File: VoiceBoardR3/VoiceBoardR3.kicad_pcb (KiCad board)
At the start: 4 copper layers, 130 x 50 mm, 170 parts, among them Q201 BC857, Q202 BC857, Q301 BC858, Q302 BC858, Q401 BC857, Q402 BC857, Q403 BC847, Q404 BC857, Q405 BC847, Q406 BC857, U101 TMUX4053, U102 TMUX4053, U103 VoiceBoardConn_18P_254P, U201 TL074, U202 TL074, U203 MCP4451-104E-ST, U204 TL074, U205 MCP4451-104E-ST, U206 TL072, U301 TL074, U302 MCP45HV51-ST, U303 LM13700, U402 LM13700, U403 TL074, U404 TL074

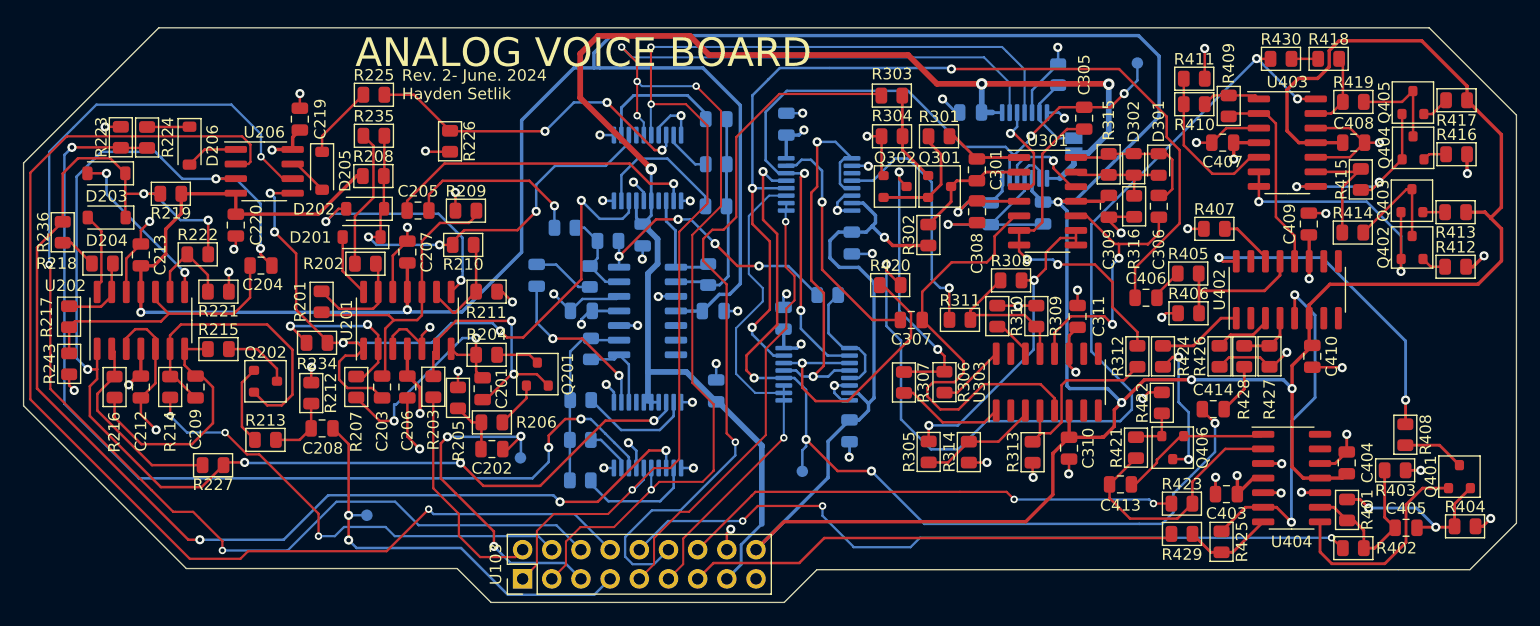
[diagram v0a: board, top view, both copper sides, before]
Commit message: separate power supply board
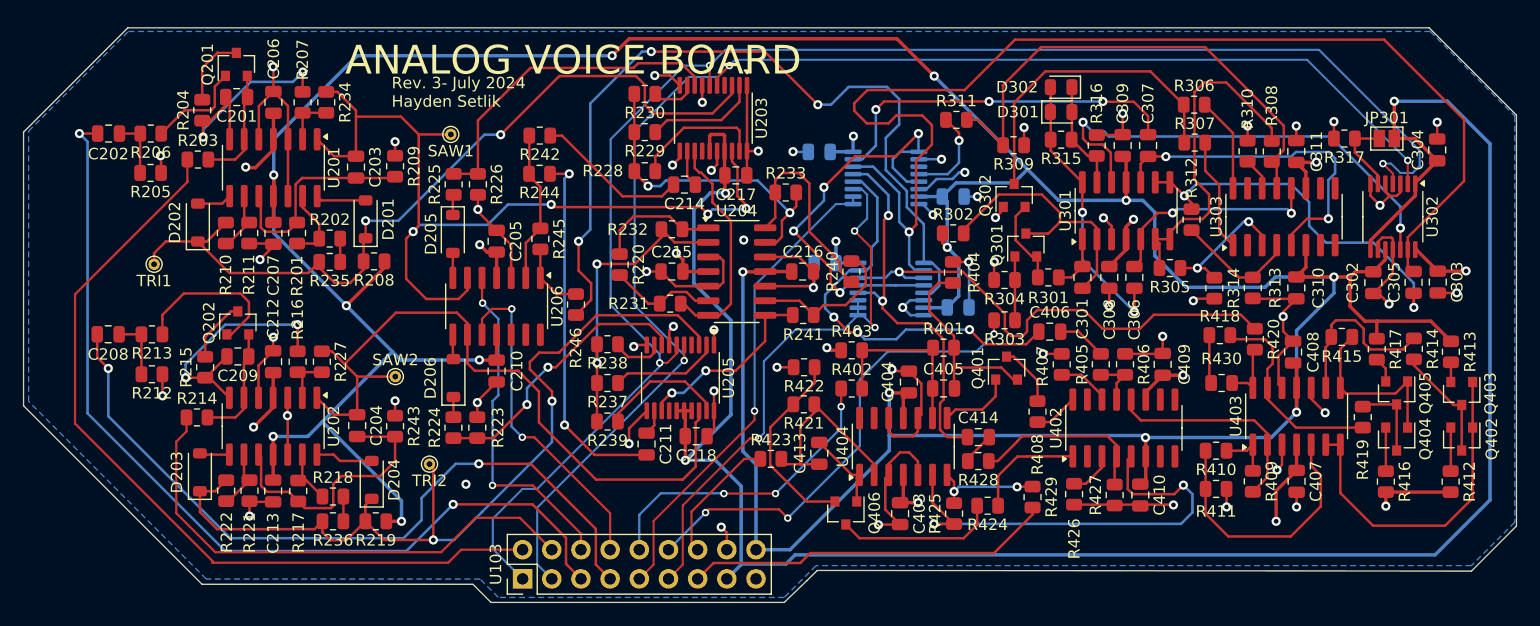
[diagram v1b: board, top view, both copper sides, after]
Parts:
- removed C219, C220: 100n, Capacitor_SMD:C_0805_2012Metric
- removed TP101: FLTR_OUT, TestPoint:TestPoint_Pad_D1.0mm_Value
- removed TP102: VCA_IN, TestPoint:TestPoint_Pad_D1.0mm_Value
- removed TP103: CLK_2, TestPoint:TestPoint_Pad_D1.0mm_Value
- removed TP104: CLK_1, TestPoint:TestPoint_Pad_D1.0mm_Value
- added C211: 1u, Capacitor_SMD:C_0805_2012Metric, F.Cu at (54.2, 36.1)
- added C214: 1u, Capacitor_SMD:C_0805_2012Metric, F.Cu at (57.5, 13.6)
- added R220: 100k, Resistor_SMD:R_0805_2012Metric, F.Cu at (51.9, 20.5)
- added R244: 10k, Resistor_SMD:R_0805_2012Metric, F.Cu at (44.9, 12.6)
- added R245: 56k, Resistor_SMD:R_0805_2012Metric, F.Cu at (45.0, 18.3)
- added R246: 470, Resistor_SMD:R_0805_2012Metric, F.Cu at (48.1, 24.0)
- added SAW1: SAW1_DC, TestPoint:TestPoint_THTPad_D1.0mm_Drill0.5mm, F.Cu at (37.2, 9.19)
- added SAW2: SAW2_DC, TestPoint:TestPoint_THTPad_D1.0mm_Drill0.5mm, F.Cu at (32.4, 30.3)
- added TRI1: SAW1_DC, TestPoint:TestPoint_THTPad_D1.0mm_Drill0.5mm, F.Cu at (11.4, 20.5)
- added TRI2: SAW1_DC, TestPoint:TestPoint_THTPad_D1.0mm_Drill0.5mm, F.Cu at (35.3, 37.9)
- C205: value 1u -> 100n
- C210: value 1u -> 100n; moved to F.Cu
- C215, C216, C217, C218, C302, C303, C304, JP301, U203, U204, U205, U302: moved to F.Cu
- Q201, Q202, Q401, Q402, Q403, Q404, Q405, Q406: footprint PCM_Package_TO_SOT_SMD_AKL:SOT-23 -> PCM_4ms_Package_SOT:SOT-23
- Q301, Q302: value BC858 -> BC857; footprint PCM_Package_TO_SOT_SMD_AKL:SOT-23 -> PCM_4ms_Package_SOT:SOT-23
- R201, R202, R203, R204, R205, R206, R207, R208, R209, R210, R211, R212, R213, R214, R215, R216, R217, R218, R219, R221, R222, R223, R224, R225, R226, R227, R234, R235, R236, R243, R301, R302, R303, R304, R305, R306, R307, R308, R309, R310, R311, R312, R313, R314, R315, R316, R401, R402, R403, R404, R405, R406, R407, R408, R409, R410, R411, R412, R413, R414, R415, R416, R417, R418, R419, R420, R421, R422, R423, R424, R425, R426, R427, R428, R429, R430: footprint PCM_Resistor_SMD_AKL:R_0805_2012Metric -> Resistor_SMD:R_0805_2012Metric
- R228, R229, R230, R237, R238, R239, R241, R317: footprint PCM_Resistor_SMD_AKL:R_0805_2012Metric -> Resistor_SMD:R_0805_2012Metric; moved to F.Cu
- R231, R240: value 220k -> 100k; footprint PCM_Resistor_SMD_AKL:R_0805_2012Metric -> Resistor_SMD:R_0805_2012Metric; moved to F.Cu
- R232, R233: value 100k -> 33k; footprint PCM_Resistor_SMD_AKL:R_0805_2012Metric -> Resistor_SMD:R_0805_2012Metric; moved to F.Cu
- R242: value 1k -> 10k; footprint PCM_Resistor_SMD_AKL:R_0805_2012Metric -> Resistor_SMD:R_0805_2012Metric; moved to F.Cu
- U206: value TL072 -> TL074; footprint Package_SO:SOIC-8_3.9x4.9mm_P1.27mm -> Package_SO:SOIC-14_3.9x8.7mm_P1.27mm
- moved R404 49.8 mm to (80.9, 21.2), turned to 90 degrees
- moved R403 48.5 mm to (72.1, 28.0), turned to 0 degrees
- moved R402 45.8 mm to (72.1, 31.3)
- moved C202 43.2 mm to (7.39, 9.12), turned to 0 degrees
- moved C405 42.1 mm to (80.1, 31.3)
- moved C304 40.8 mm to (123.1, 10.5), turned to 90 degrees
- moved Q401 40.5 mm to (85.6, 29.5)
- moved R223 40.0 mm to (39.5, 34.7)
- moved C303 39.4 mm to (123.1, 22.0)
- moved R206 38.9 mm to (11.1, 9.12)
- moved C404 38.8 mm to (77.1, 30.7)
- moved R401 37.9 mm to (80.1, 27.8), turned to 0 degrees
- moved Q201 37.6 mm to (18.5, 3.10)
- moved R224 36.7 mm to (37.4, 34.7)
- moved R423 36.0 mm to (65.0, 37.4)
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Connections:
- C205 pad 1: Net-(U203A-P0W) -> GND
- C205 pad 2: Net-(C205-Pad2) -> +12V
- C210 pad 1: Net-(U205A-P0W) -> GND
- C210 pad 2: Net-(C210-Pad2) -> -12V
- C305 pad 1: Net-(U301B--) -> Net-(U301C--)
- C306 pad 1: Net-(U301C-+) -> Net-(U301B-+)
- C307 pad 1: Net-(U301B-+) -> Net-(U301C-+)
- R228 pad 2: Net-(U204C--) -> Net-(U204D--)
- R229 pad 2: Net-(U204C--) -> Net-(U204D--)
- R230 pad 2: Net-(U204C--) -> Net-(U204D--)
- R231 pad 1: Net-(C205-Pad2) -> Net-(U204B--)
- R231 pad 2: Net-(U204B--) -> Net-(U203A-P0B)
- R232 pad 2: Net-(U205A-P0B) -> Net-(R220-Pad1)
- R233 pad 1: Net-(U204C--) -> Net-(U204D--)
- R233 pad 2: Net-(U203A-P0B) -> Net-(R233-Pad2)
- R240 pad 1: Net-(C210-Pad2) -> Net-(R233-Pad2)
- R240 pad 2: Net-(U204B--) -> Net-(U204C--)
- R241 pad 1: Net-(U204B--) -> Net-(U204C--)
- R241 pad 2: Net-(R241-Pad2) -> Net-(U205A-P0B)
- R242 pad 1: Net-(R241-Pad2) -> Net-(C214-Pad2)
- R242 pad 2: OSC_MIX -> Net-(U206A--)
- R305 pad 2: Net-(U301C--) -> Net-(U301B--)
- R308 pad 2: Net-(U301C--) -> Net-(U301B--)
- R312 pad 2: Net-(U301B--) -> Net-(U301C--)
- U204 pad 1: Net-(U205A-P0B) -> Net-(R220-Pad1)
- U204 pad 12: unconnected-(U204D-+-Pad12) -> GND
- U204 pad 13: unconnected-(U204D---Pad13) -> Net-(U204D--)
- U204 pad 14: unconnected-(U204-Pad14) -> Net-(R233-Pad2)
- U204 pad 7: Net-(R241-Pad2) -> Net-(U203A-P0B)
- U204 pad 8: Net-(U203A-P0B) -> Net-(U205A-P0B)
- U206 pad 1: Net-(D206-A) -> Net-(R245-Pad2)
- U206 pad 2: PWM_2_CV -> Net-(U206A--)
- U206 pad 3: SAW2_FULL -> GND
- U206 pad 4: -12V -> +12V
- U206 pad 5: SAW1_FULL -> PWM_1_CV
- U206 pad 6: PWM_1_CV -> SAW1_FULL
- U206 pad 8: +12V -> Net-(D206-A)
- U303 pad 12: Net-(U301C-+) -> Net-(U301B-+)
- U303 pad 5: Net-(U301B-+) -> Net-(U301C-+)
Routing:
- net Net-(R420-Pad2): track 84.8 -> 5.37 mm, vias 3 -> 0
- net PWM_1_CV: track 103.4 -> 29.7 mm, vias 3 -> 2
- net PWM_2_CV: track 102.9 -> 29.5 mm, vias 1 -> 2
- net -12V: track 421.0 -> 347.9 mm, vias 7 -> 14
- net PULSE2_FULL: track 86.8 -> 24.3 mm, vias 3 -> 2
- net OSC_MIX: track 10.7 -> 72.3 mm, vias 0 -> 3
- net +3.3V: track 127.7 -> 182.4 mm
- net LEVEL_1_CV: track 19.6 -> 71.6 mm
- net CLK_1: track 30.8 -> 79.9 mm, vias 3 -> 2
- net FOLDER_IN: track 85.2 -> 36.1 mm
- net VCA_IN: track 80.8 -> 33.4 mm, vias 5 -> 2
- net SAW2_FULL: track 108.4 -> 62.3 mm, vias 6 -> 0
- net FOLD_CV: track 65.5 -> 27.2 mm
- net FILTER_OUT: track 68.9 -> 105.4 mm, vias 4 -> 1
- net SDA: track 102.6 -> 136.7 mm
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- added copper zone on B.Cu, net GND
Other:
- outline, holes or cut-outs redrawn
- board text added: "Rev. 3- July 2024 Hayden Setlik"
- board text removed: "Rev. 2- June. 2024 Hayden Setlik"

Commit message: Power Supply rev2
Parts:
- R223: value 39k -> 47k
- R224: value 92k -> 100k
- R226: value 39k -> 100k
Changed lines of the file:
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@@
 			)
 		)
-		(property "Value" "92k"
+		(property "Value" "100k"
 			(at 0 1.65 90)
 			(layer "F.Fab")
@@
 			)
 		)
-		(property "Value" "39k"
+		(property "Value" "47k"
 			(at 0 1.65 90)
 			(layer "F.Fab")
@@
 			)
 		)
-		(property "Value" "39k"
+		(property "Value" "100k"
 			(at 0 1.65 90)
 			(layer "F.Fab")
